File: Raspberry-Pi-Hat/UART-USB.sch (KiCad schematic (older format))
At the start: 8 parts, among them U6 MCP2221AxSL

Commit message: Starting placing component
Assigned component footprint and started placing component on the board
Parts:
- C19, C20: footprint Capacitor_SMD:C_0603_1608Metric_Pad1.05x0.95mm_HandSolder -> Capacitor_SMD:C_1206_3216Metric_Pad1.42x1.75mm_HandSolder
- R19, R20, R21: footprint (none) -> Resistor_SMD:R_0603_1608Metric_Pad1.05x0.95mm_HandSolder
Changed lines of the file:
@@
 $Descr A4 11693 8268
 encoding utf-8
-Sheet 3 4
+Sheet 4 4
 Title ""
 Date ""
@@
 F 0 "R22" H 5041 2904 50  0000 R CNN
 F 1 "5k" H 5041 2995 50  0000 R CNN
-F 2 "" H 5100 2950 50  0001 C CNN
+F 2 "Resistor_SMD:R_0603_1608Metric_Pad1.05x0.95mm_HandSolder" H 5100 2950 50  0001 C CNN
 F 3 "~" H 5100 2950 50  0001 C CNN
 	1    5100 2950
@@
 F 0 "C21" H 4865 2996 50  0000 L CNN
 F 1 "C" H 4865 2905 50  0000 L CNN
-F 2 "Capacitor_SMD:C_0603_1608Metric_Pad1.05x0.95mm_HandSolder" H 4788 2800 50  0001 C CNN
+F 2 "Capacitor_SMD:C_1206_3216Metric_Pad1.42x1.75mm_HandSolder" H 4788 2800 50  0001 C CNN
 F 3 "~" H 4750 2950 50  0001 C CNN
 	1    4750 2950
@@
 F 0 "C22" H 6865 3046 50  0000 L CNN
 F 1 "C" H 6865 2955 50  0000 L CNN
-F 2 "Capacitor_SMD:C_0603_1608Metric_Pad1.05x0.95mm_HandSolder" H 6788 2850 50  0001 C CNN
+F 2 "Capacitor_SMD:C_1206_3216Metric_Pad1.42x1.75mm_HandSolder" H 6788 2850 50  0001 C CNN
 F 3 "~" H 6750 3000 50  0001 C CNN
 	1    6750 3000
@@
 F 0 "R26" H 7491 3104 50  0000 R CNN
 F 1 "R_small" H 7491 3195 50  0000 R CNN
-F 2 "" H 7550 3150 50  0001 C CNN
+F 2 "Resistor_SMD:R_0603_1608Metric_Pad1.05x0.95mm_HandSolder" H 7550 3150 50  0001 C CNN
 F 3 "~" H 7550 3150 50  0001 C CNN
 	1    7550 3150
@@
 F 0 "R25" H 7091 3104 50  0000 R CNN
 F 1 "R_small" H 7091 3195 50  0000 R CNN
-F 2 "" H 7150 3150 50  0001 C CNN
+F 2 "Resistor_SMD:R_0603_1608Metric_Pad1.05x0.95mm_HandSolder" H 7150 3150 50  0001 C CNN
 F 3 "~" H 7150 3150 50  0001 C CNN
 	1    7150 3150

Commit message: changed footprint size
changed resistor and capacitor footprint size for 0603 when possible.
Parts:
- C19, C20: footprint Capacitor_SMD:C_1206_3216Metric_Pad1.42x1.75mm_HandSolder -> Capacitor_SMD:C_0603_1608Metric_Pad1.05x0.95mm_HandSolder
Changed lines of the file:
@@
 F 0 "C21" H 4865 2996 50  0000 L CNN
 F 1 "C" H 4865 2905 50  0000 L CNN
-F 2 "Capacitor_SMD:C_1206_3216Metric_Pad1.42x1.75mm_HandSolder" H 4788 2800 50  0001 C CNN
+F 2 "Capacitor_SMD:C_0603_1608Metric_Pad1.05x0.95mm_HandSolder" H 4788 2800 50  0001 C CNN
 F 3 "~" H 4750 2950 50  0001 C CNN
 	1    4750 2950
@@
 F 0 "C22" H 6865 3046 50  0000 L CNN
 F 1 "C" H 6865 2955 50  0000 L CNN
-F 2 "Capacitor_SMD:C_1206_3216Metric_Pad1.42x1.75mm_HandSolder" H 6788 2850 50  0001 C CNN
+F 2 "Capacitor_SMD:C_0603_1608Metric_Pad1.05x0.95mm_HandSolder" H 6788 2850 50  0001 C CNN
 F 3 "~" H 6750 3000 50  0001 C CNN
 	1    6750 3000

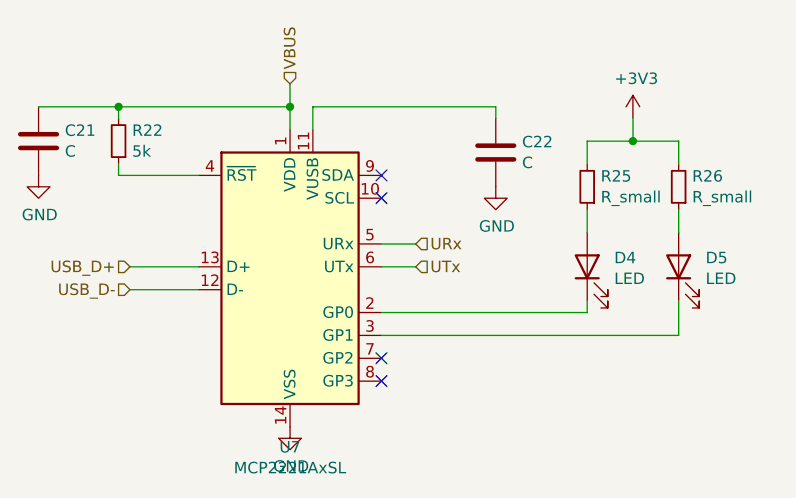
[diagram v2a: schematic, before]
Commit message: Routted diff pair
All USB lines is routed and most of the signal lines is routed as well.
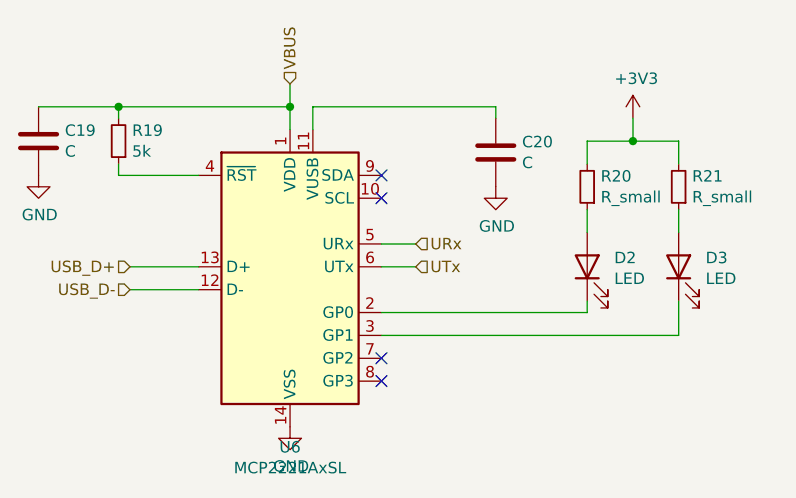
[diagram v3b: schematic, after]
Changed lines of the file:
@@
 $Descr A4 11693 8268
 encoding utf-8
-Sheet 4 4
+Sheet 3 4
 Title ""
 Date ""
@@
 AR Path="/5ED9C277/5ED897A3" Ref="U?"  Part="1"
 AR Path="/5EF4B9E7/5ED897A3" Ref="U7"  Part="1"
-F 0 "U7" H 5850 2911 50  0000 C CNN
+F 0 "U6" H 5850 2911 50  0000 C CNN
 F 1 "MCP2221AxSL" H 5850 2820 50  0000 C CNN
 F 2 "Package_SO:SOIC-14_3.9x8.7mm_P1.27mm" H 5850 4600 50  0001 C CNN
@@
 AR Path="/5ED9C277/5ED8AD4E" Ref="D?"  Part="1"
 AR Path="/5EF4B9E7/5ED8AD4E" Ref="D4"  Part="1"
-F 0 "D4" V 7189 3382 50  0000 R CNN
+F 0 "D2" V 7189 3382 50  0000 R CNN
 F 1 "LED" V 7098 3382 50  0000 R CNN
 F 2 "LED_SMD:LED_0603_1608Metric" H 7150 3500 50  0001 C CNN
@@
 AR Path="/5ED9C277/5ED8D572" Ref="D?"  Part="1"
 AR Path="/5EF4B9E7/5ED8D572" Ref="D5"  Part="1"
-F 0 "D5" V 7589 3382 50  0000 R CNN
+F 0 "D3" V 7589 3382 50  0000 R CNN
 F 1 "LED" V 7498 3382 50  0000 R CNN
 F 2 "LED_SMD:LED_0603_1608Metric" H 7550 3500 50  0001 C CNN
@@
 AR Path="/5ED9C277/5ED8DC94" Ref="R?"  Part="1"
 AR Path="/5EF4B9E7/5ED8DC94" Ref="R22"  Part="1"
-F 0 "R22" H 5041 2904 50  0000 R CNN
+F 0 "R19" H 5041 2904 50  0000 R CNN
 F 1 "5k" H 5041 2995 50  0000 R CNN
 F 2 "Resistor_SMD:R_0603_1608Metric_Pad1.05x0.95mm_HandSolder" H 5100 2950 50  0001 C CNN
@@
 AR Path="/5ED9C277/5ED8F339" Ref="C?"  Part="1"
 AR Path="/5EF4B9E7/5ED8F339" Ref="C21"  Part="1"
-F 0 "C21" H 4865 2996 50  0000 L CNN
+F 0 "C19" H 4865 2996 50  0000 L CNN
 F 1 "C" H 4865 2905 50  0000 L CNN
 F 2 "Capacitor_SMD:C_0603_1608Metric_Pad1.05x0.95mm_HandSolder" H 4788 2800 50  0001 C CNN
@@
 AR Path="/5ED9C277/5ED9055B" Ref="C?"  Part="1"
 AR Path="/5EF4B9E7/5ED9055B" Ref="C22"  Part="1"
-F 0 "C22" H 6865 3046 50  0000 L CNN
+F 0 "C20" H 6865 3046 50  0000 L CNN
 F 1 "C" H 6865 2955 50  0000 L CNN
 F 2 "Capacitor_SMD:C_0603_1608Metric_Pad1.05x0.95mm_HandSolder" H 6788 2850 50  0001 C CNN
@@
 AR Path="/5ED9C277/5ED952F6" Ref="R?"  Part="1"
 AR Path="/5EF4B9E7/5ED952F6" Ref="R26"  Part="1"
-F 0 "R26" H 7491 3104 50  0000 R CNN
+F 0 "R21" H 7491 3104 50  0000 R CNN
 F 1 "R_small" H 7491 3195 50  0000 R CNN
 F 2 "Resistor_SMD:R_0603_1608Metric_Pad1.05x0.95mm_HandSolder" H 7550 3150 50  0001 C CNN
@@
 AR Path="/5ED9C277/5ED95D2E" Ref="R?"  Part="1"
 AR Path="/5EF4B9E7/5ED95D2E" Ref="R25"  Part="1"
-F 0 "R25" H 7091 3104 50  0000 R CNN
+F 0 "R20" H 7091 3104 50  0000 R CNN
 F 1 "R_small" H 7091 3195 50  0000 R CNN
 F 2 "Resistor_SMD:R_0603_1608Metric_Pad1.05x0.95mm_HandSolder" H 7150 3150 50  0001 C CNN

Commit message: Change strategy
Remove USB hub, connect CAN to SPI and NMEA to RSPI serial.
Addition of RTC
Addition of Fan PWM connector
Plan to add a soft start button
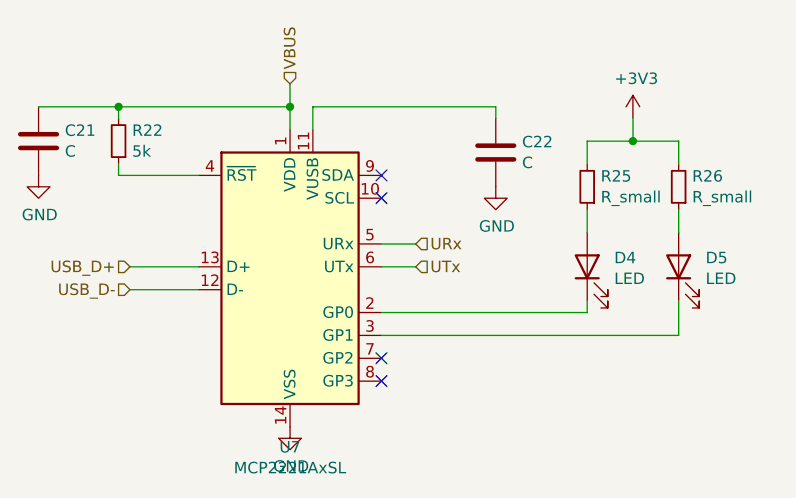
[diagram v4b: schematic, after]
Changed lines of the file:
@@
 $Descr A4 11693 8268
 encoding utf-8
-Sheet 3 4
+Sheet 4 4
 Title ""
 Date ""
@@
 AR Path="/5ED9C277/5ED897A3" Ref="U?"  Part="1"
 AR Path="/5EF4B9E7/5ED897A3" Ref="U7"  Part="1"
-F 0 "U6" H 5850 2911 50  0000 C CNN
+F 0 "U7" H 5850 2911 50  0000 C CNN
 F 1 "MCP2221AxSL" H 5850 2820 50  0000 C CNN
 F 2 "Package_SO:SOIC-14_3.9x8.7mm_P1.27mm" H 5850 4600 50  0001 C CNN
@@
 AR Path="/5ED9C277/5ED8AD4E" Ref="D?"  Part="1"
 AR Path="/5EF4B9E7/5ED8AD4E" Ref="D4"  Part="1"
-F 0 "D2" V 7189 3382 50  0000 R CNN
+F 0 "D4" V 7189 3382 50  0000 R CNN
 F 1 "LED" V 7098 3382 50  0000 R CNN
 F 2 "LED_SMD:LED_0603_1608Metric" H 7150 3500 50  0001 C CNN
@@
 AR Path="/5ED9C277/5ED8D572" Ref="D?"  Part="1"
 AR Path="/5EF4B9E7/5ED8D572" Ref="D5"  Part="1"
-F 0 "D3" V 7589 3382 50  0000 R CNN
+F 0 "D5" V 7589 3382 50  0000 R CNN
 F 1 "LED" V 7498 3382 50  0000 R CNN
 F 2 "LED_SMD:LED_0603_1608Metric" H 7550 3500 50  0001 C CNN
@@
 AR Path="/5ED9C277/5ED8DC94" Ref="R?"  Part="1"
 AR Path="/5EF4B9E7/5ED8DC94" Ref="R22"  Part="1"
-F 0 "R19" H 5041 2904 50  0000 R CNN
+F 0 "R22" H 5041 2904 50  0000 R CNN
 F 1 "5k" H 5041 2995 50  0000 R CNN
 F 2 "Resistor_SMD:R_0603_1608Metric_Pad1.05x0.95mm_HandSolder" H 5100 2950 50  0001 C CNN
@@
 AR Path="/5ED9C277/5ED8F339" Ref="C?"  Part="1"
 AR Path="/5EF4B9E7/5ED8F339" Ref="C21"  Part="1"
-F 0 "C19" H 4865 2996 50  0000 L CNN
+F 0 "C21" H 4865 2996 50  0000 L CNN
 F 1 "C" H 4865 2905 50  0000 L CNN
 F 2 "Capacitor_SMD:C_0603_1608Metric_Pad1.05x0.95mm_HandSolder" H 4788 2800 50  0001 C CNN
@@
 AR Path="/5ED9C277/5ED9055B" Ref="C?"  Part="1"
 AR Path="/5EF4B9E7/5ED9055B" Ref="C22"  Part="1"
-F 0 "C20" H 6865 3046 50  0000 L CNN
+F 0 "C22" H 6865 3046 50  0000 L CNN
 F 1 "C" H 6865 2955 50  0000 L CNN
 F 2 "Capacitor_SMD:C_0603_1608Metric_Pad1.05x0.95mm_HandSolder" H 6788 2850 50  0001 C CNN
@@
 AR Path="/5ED9C277/5ED952F6" Ref="R?"  Part="1"
 AR Path="/5EF4B9E7/5ED952F6" Ref="R26"  Part="1"
-F 0 "R21" H 7491 3104 50  0000 R CNN
+F 0 "R26" H 7491 3104 50  0000 R CNN
 F 1 "R_small" H 7491 3195 50  0000 R CNN
 F 2 "Resistor_SMD:R_0603_1608Metric_Pad1.05x0.95mm_HandSolder" H 7550 3150 50  0001 C CNN
@@
 AR Path="/5ED9C277/5ED95D2E" Ref="R?"  Part="1"
 AR Path="/5EF4B9E7/5ED95D2E" Ref="R25"  Part="1"
-F 0 "R20" H 7091 3104 50  0000 R CNN
+F 0 "R25" H 7091 3104 50  0000 R CNN
 F 1 "R_small" H 7091 3195 50  0000 R CNN
 F 2 "Resistor_SMD:R_0603_1608Metric_Pad1.05x0.95mm_HandSolder" H 7150 3150 50  0001 C CNN
